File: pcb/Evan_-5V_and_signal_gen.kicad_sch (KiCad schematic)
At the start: 29 parts, among them IC1 TL7660IDGKR, IC4 UA78M33CDCYG3, IC9 TL081IDT, U5 TPS2069CDBVR_MOSFET

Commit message: Changed C18, C19, C20, C28, C32, C34, C38, C41, C46, C47 footprints to 0805
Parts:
- C18, C41, C46: footprint capstone:CAPC220145_88N_KEM-0.1u -> Capacitor_SMD:C_0805_2012Metric
- C47: footprint Capacitor_SMD:C_0402_1005Metric -> Capacitor_SMD:C_0805_2012Metric
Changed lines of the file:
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@@
 			)
 		)
-		(property "Footprint" "Capacitor_SMD:C_0402_1005Metric"
+		(property "Footprint" "Capacitor_SMD:C_0805_2012Metric"
 			(at 169.8752 57.15 0)
 			(effects
@@
 			)
 		)
-		(property "Footprint" "capstone:CAPC220145_88N_KEM-0.1u"
+		(property "Footprint" "Capacitor_SMD:C_0805_2012Metric"
 			(at 256.54 68.58 0)
 			(effects
@@
 			)
 		)
-		(property "Footprint" "capstone:CAPC220145_88N_KEM-0.1u"
+		(property "Footprint" "Capacitor_SMD:C_0805_2012Metric"
 			(at 186.69 71.12 0)
 			(effects
@@
 			)
 		)
-		(property "Footprint" "capstone:CAPC220145_88N_KEM-0.1u"
+		(property "Footprint" "Capacitor_SMD:C_0805_2012Metric"
 			(at 83.312 85.09 0)
 			(effects

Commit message: Added more to the BOM
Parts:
- C12, C13: Manufacturer_Name KEMET -> Murata; Manufacturer_Part_Number T495D106K035ATE300 -> GRT21BR61C106KE01L
- C14, C15, C16, C17: Manufacturer_Name (none) -> Murata; Manufacturer_Part_Number (none) -> GRM155R61C474KE01D
- C18, C26, C41, C46: Manufacturer_Name (none) -> KEMET; Manufacturer_Part_Number (none) -> C0805C103K4RACAUTO
- C25: Manufacturer_Part_Number C0805C334K3RACAUTO7210 -> C0805C334K4RACAUTO
- C43: Manufacturer_Name (none) -> Murata; Manufacturer_Part_Number (none) -> GCM155R71H103KA55D
- C47: Manufacturer_Name (none) -> KEMET; Manufacturer_Part_Number (none) -> C0805C475K4RACAUTO
- R11: Manufacturer_Name (none) -> Panasonic; Manufacturer_Part_Number (none) -> ERJ-2RKF1001X
- R12: Manufacturer_Name (none) -> Panasonic; Manufacturer_Part_Number (none) -> ERJ-H2RF1002X
- R32: Manufacturer_Name (none) -> Panasonic; Manufacturer_Part_Number (none) -> ERJ-2RKF5601X
- R33: Manufacturer_Name (none) -> Panasonic; Manufacturer_Part_Number (none) -> ERJ-2RKF2000X
- R5, R6, R7, R8: Manufacturer_Name (none) -> Panasonic; Manufacturer_Part_Number (none) -> ERJ-H2RF3301X

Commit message: Finished BOM and fixed file paths for 3D models
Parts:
- H1, H2: value ESQ-126-39-L-D -> ESQ-126-39-G-D; Manufacturer_Part_Number ESQ-126-39-L-D -> ESQ-126-39-G-D
- IC9: Manufacturer_Part_Number TL081IDT -> TL081HIDR
- J_SIG1: now not fitted
- U5: Manufacturer_Name (none) -> Texas Instruments; Manufacturer_Part_Number (none) -> TPS2069CDBVR
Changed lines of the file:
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@@
 			)
 		)
-		(property "Value" "ESQ-126-39-L-D"
+		(property "Value" "ESQ-126-39-G-D"
 			(at 84.836 185.42 90)
 			(effects
@@
 			)
 		)
-		(property "Manufacturer_Part_Number" "ESQ-126-39-L-D"
+		(property "Manufacturer_Part_Number" "ESQ-126-39-G-D"
 			(at 77.47 -609.5 0)
 			(effects
@@
 			)
 		)
-		(property "Manufacturer_Part_Number" "TL081IDT"
+		(property "Manufacturer_Part_Number" "TL081HIDR"
 			(at 242.57 855.88 0)
 			(effects
@@
 		(in_bom yes)
 		(on_board yes)
-		(dnp no)
+		(dnp yes)
 		(property "Reference" "J_SIG1"
 			(at 121.666 91.44 0)
@@
 			)
 		)
-		(property "Value" "ESQ-126-39-L-D"
+		(property "Value" "ESQ-126-39-G-D"
 			(at 40.386 184.15 90)
 			(effects
@@
 			)
 		)
-		(property "Manufacturer_Part_Number" "ESQ-126-39-L-D"
+		(property "Manufacturer_Part_Number" "ESQ-126-39-G-D"
 			(at 33.02 -609.5 0)
 			(effects
@@
 			(at 34.29 85.09 0)
 			(effects
+				(font
+					(size 1.27 1.27)
+				)
+				(hide yes)
+			)
+		)
+		(property "Manufacturer_Name" "Texas Instruments"
+			(at 34.29 85.09 0)
+			(effects
+				(font
+					(size 1.27 1.27)
+				)
+				(hide yes)
+			)
+		)
+		(property "Manufacturer_Part_Number" "TPS2069CDBVR"
+			(at 34.29 85.09 0)
+			(effects

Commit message: updated component labels
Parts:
- renumbered IC1 to U3, IC4 to U4, IC9 to U9
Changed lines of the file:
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@@
 		(dnp no)
 		(fields_autoplaced yes)
-		(property "Reference" "IC1"
+		(property "Reference" "U3"
 			(at 53.34 24.13 0)
 			(effects
@@
 			(project "mcu_integration"
 				(path "/c0210bc3-f67f-47d8-a34e-f002a728adb2/39708197-8fe0-4b5c-ba49-65ed06982da9"
-					(reference "IC1")
+					(reference "U3")
 					(unit 1)
 				)
@@
 		(on_board yes)
 		(dnp no)
-		(property "Reference" "IC9"
+		(property "Reference" "U9"
 			(at 217.17 54.864 0)
 			(effects
@@
 			(project "mcu_integration"
 				(path "/c0210bc3-f67f-47d8-a34e-f002a728adb2/39708197-8fe0-4b5c-ba49-65ed06982da9"
-					(reference "IC9")
+					(reference "U9")
 					(unit 1)
 				)
@@
 		(dnp no)
 		(fields_autoplaced yes)
-		(property "Reference" "IC4"
+		(property "Reference" "U4"
 			(at 232.41 155.448 0)
 			(effects
@@
 			(project "mcu_integration"
 				(path "/c0210bc3-f67f-47d8-a34e-f002a728adb2/39708197-8fe0-4b5c-ba49-65ed06982da9"
-					(reference "IC4")
+					(reference "U4")
 					(unit 1)
 				)

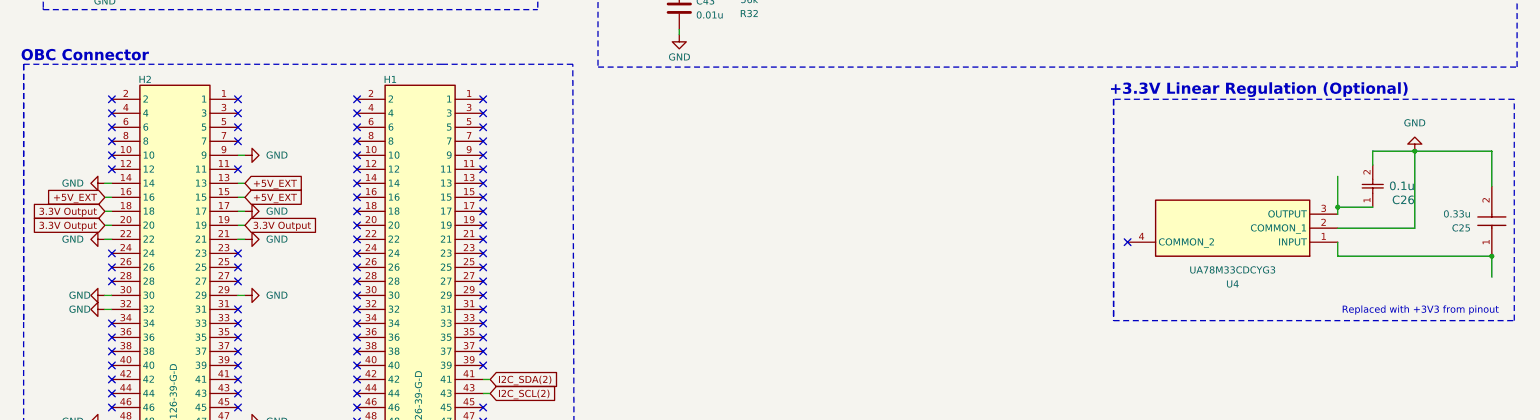
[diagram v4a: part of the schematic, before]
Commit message: Added 3.3V regulator
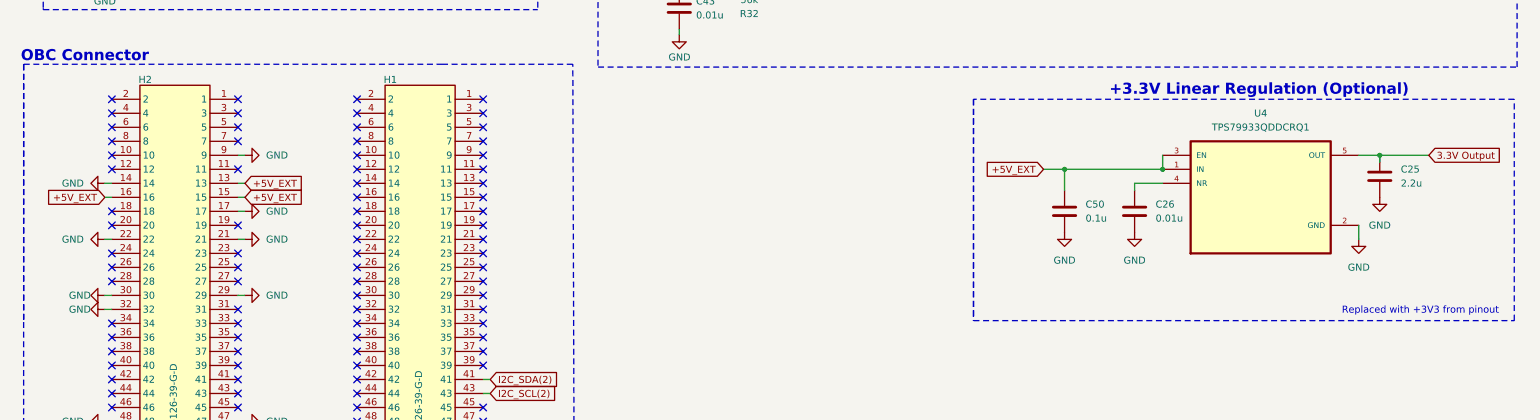
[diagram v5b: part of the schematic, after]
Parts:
- removed C25: 0.33u, capstone:C0805, symbol capstone:C0805C334K3RACAUTO7210
- removed C26: 0.1u, capstone:CAPC220145_88N_KEM-0.1u, symbol capstone:C0805C104K5RAC7210
- removed U4: UA78M33CDCYG3, capstone:SOT230P700X180-4N, symbol capstone:UA78M33CDCYG3
- added C25: 2.2u, Capacitor_SMD:C_0402_1005Metric, symbol Device:C
- added C26: 0.01u, Capacitor_SMD:C_0402_1005Metric, symbol Device:C
- added C50: 0.1u, Capacitor_SMD:C_0402_1005Metric, symbol Device:C
- added U4: TPS79933QDDCRQ1, TPS79933QDDCRQ1 (1):SOT95P280X110-5N, symbol TPS79933QDDCRQ1:TPS79933QDDCRQ1
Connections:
- net +5V_EXT: now also C50.1, U4.1 (IN), U4.3 (EN)
- net 3.3V Output: now also C25.1, U4.5 (OUT); no longer H2.18, H2.19, H2.20
- net GND: now also C25.2, C26.2, C50.2, U4.2 (GND)
- new net: C26.1, U4.4 (NR)
- no-connect marks 91 -> 93

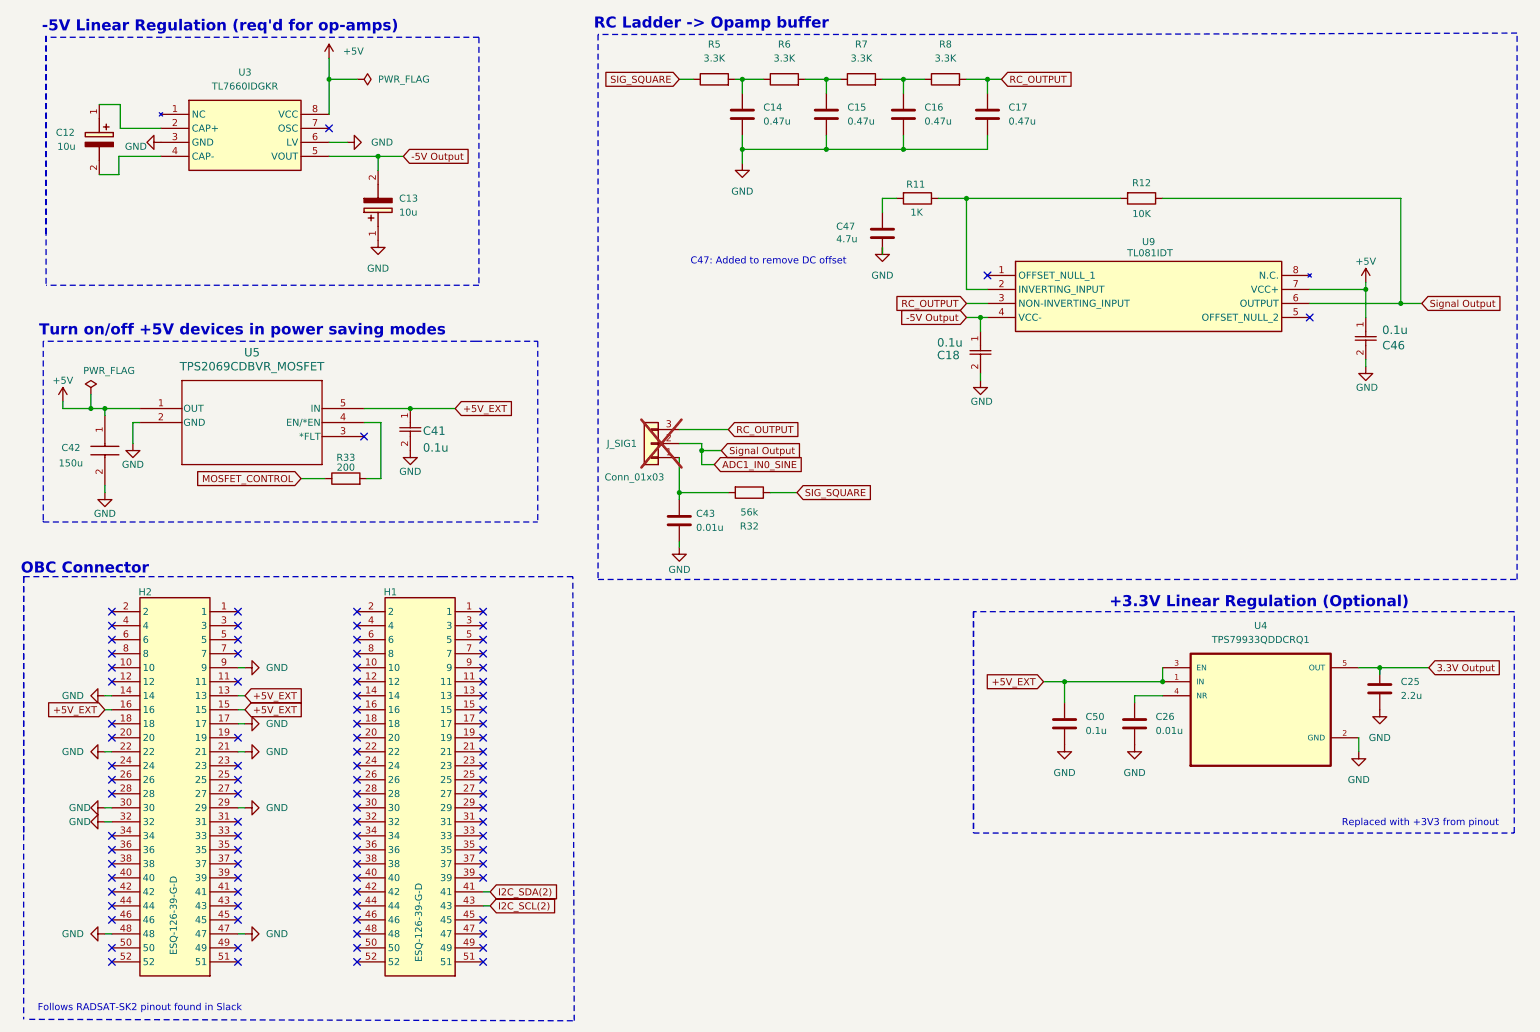
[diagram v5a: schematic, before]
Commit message: updated schematic lables
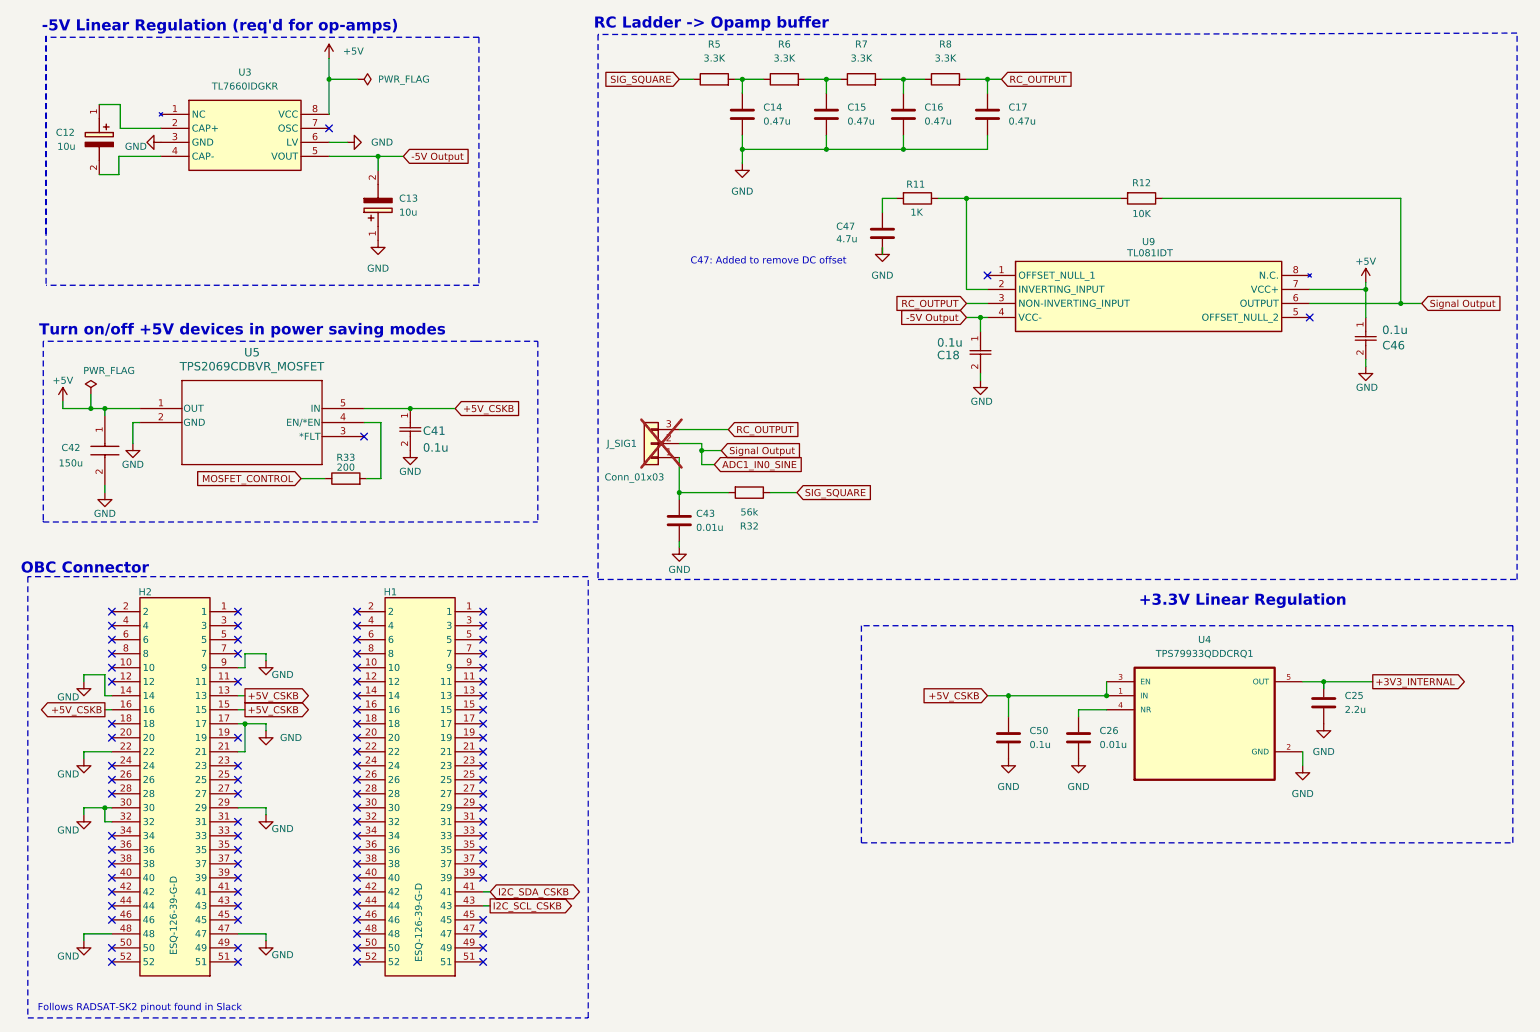
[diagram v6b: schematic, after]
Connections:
- net +5V_EXT renamed +5V_CSKB
- net 3.3V Output renamed +3V3_INTERNAL
- net I2C_SCL(2) renamed I2C_SCL_CSKB
- net I2C_SDA(2) renamed I2C_SDA_CSKB
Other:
- note added: "+3.3V Linear Regulation"
- note removed: "+3.3V Linear Regulation (Optional)"
- note removed: "Replaced with +3V3 from pinout"
- moved on the sheet: C25, C26, C50, U4

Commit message: Changed spacing of test ICs to allow for larger melanin domes
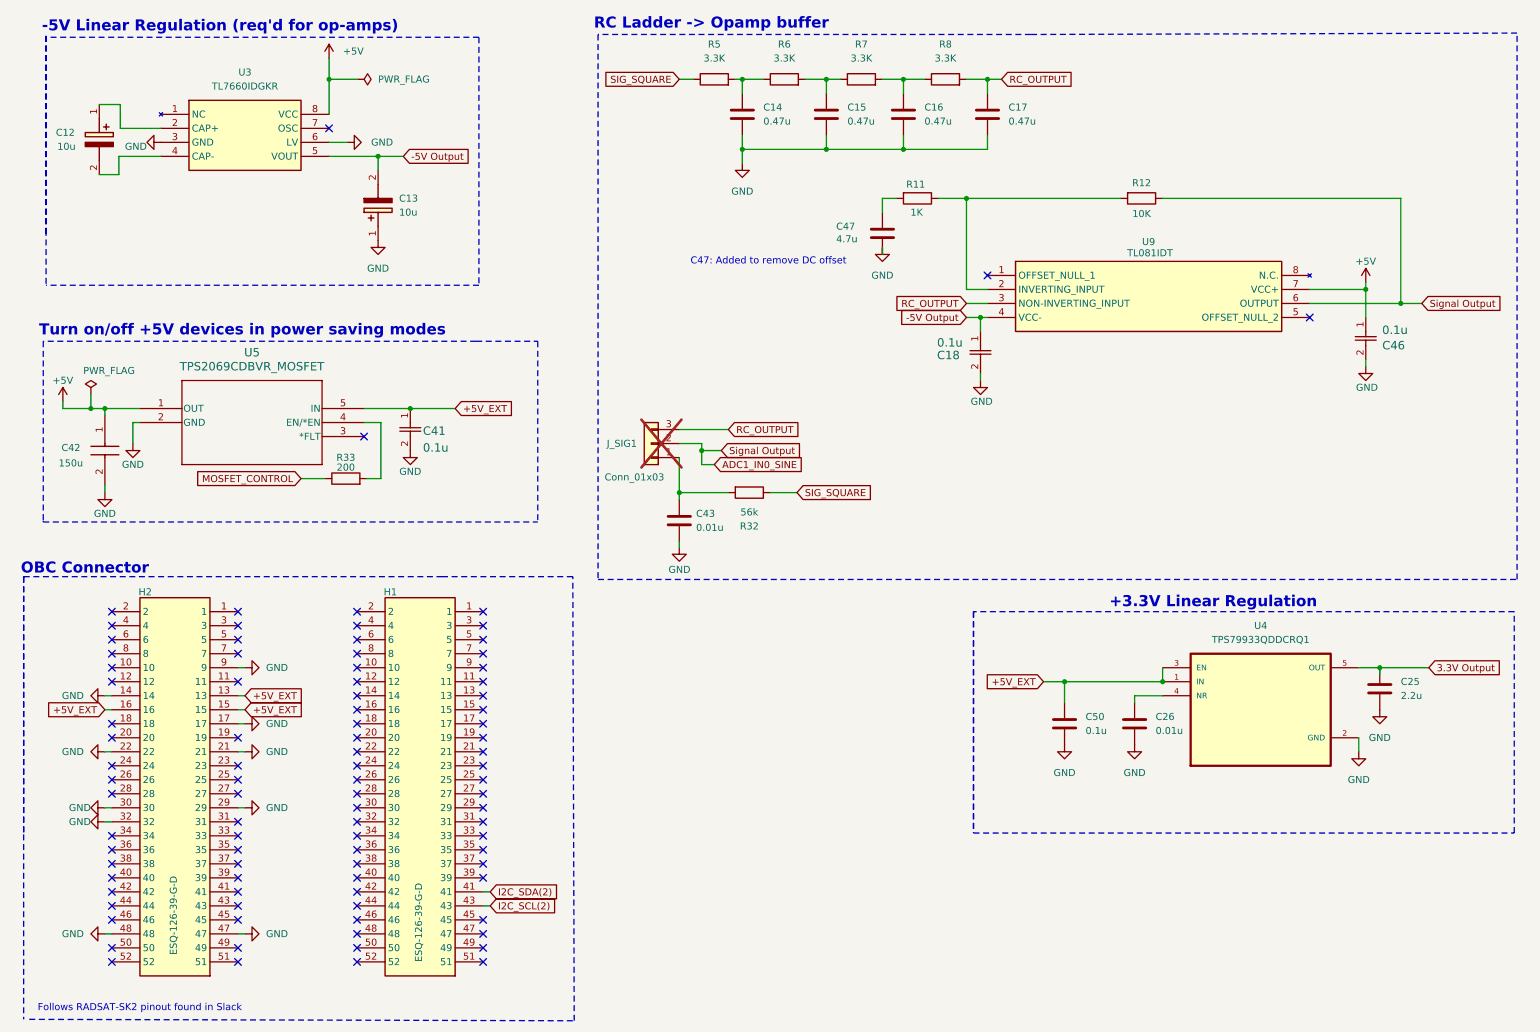
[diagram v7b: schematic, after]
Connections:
- net +3V3_INTERNAL renamed 3.3V Output
- net +5V_CSKB renamed +5V_EXT
- net I2C_SCL_CSKB renamed I2C_SCL(2)
- net I2C_SDA_CSKB renamed I2C_SDA(2)
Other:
- moved on the sheet: C25, C26, C50, U4
